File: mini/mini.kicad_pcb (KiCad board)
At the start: 2 copper layers, 1 part, among them U1 ESP32-WROOM-32E

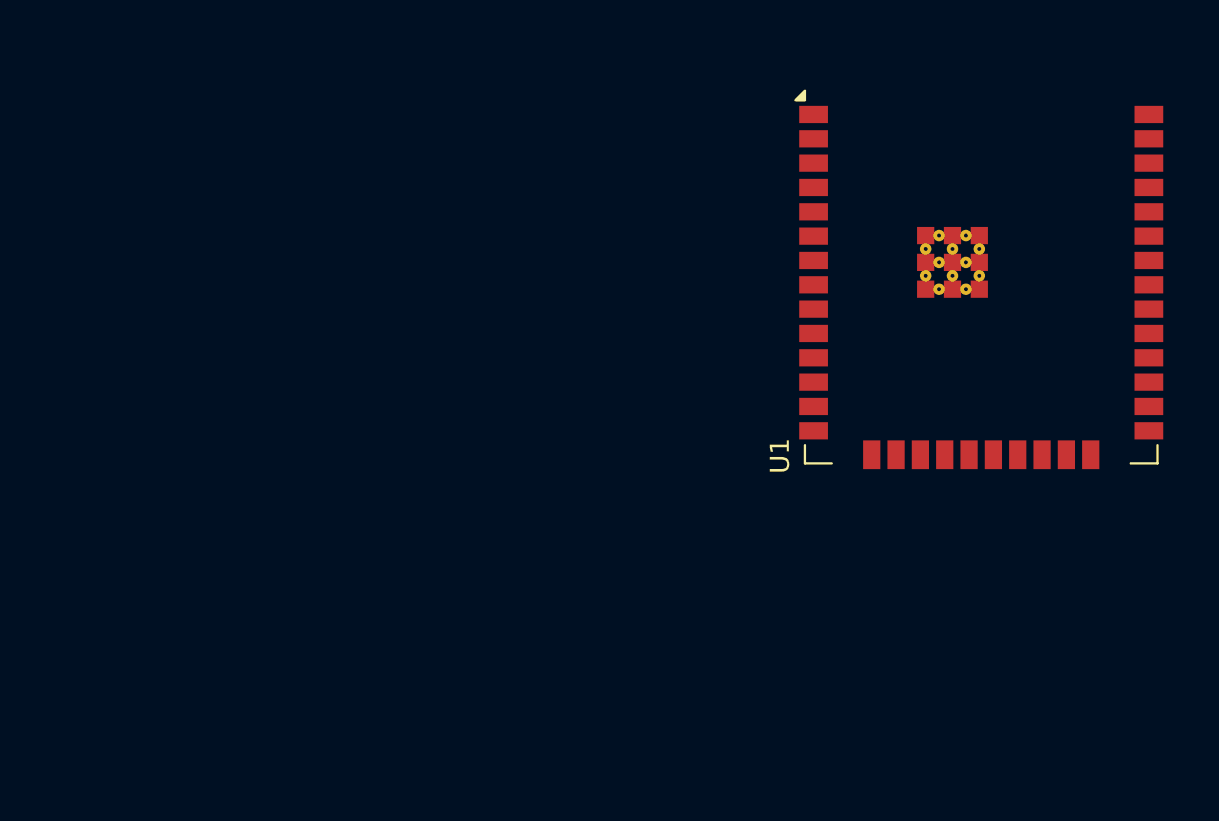
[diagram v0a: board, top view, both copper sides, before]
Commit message: Created power page schematic
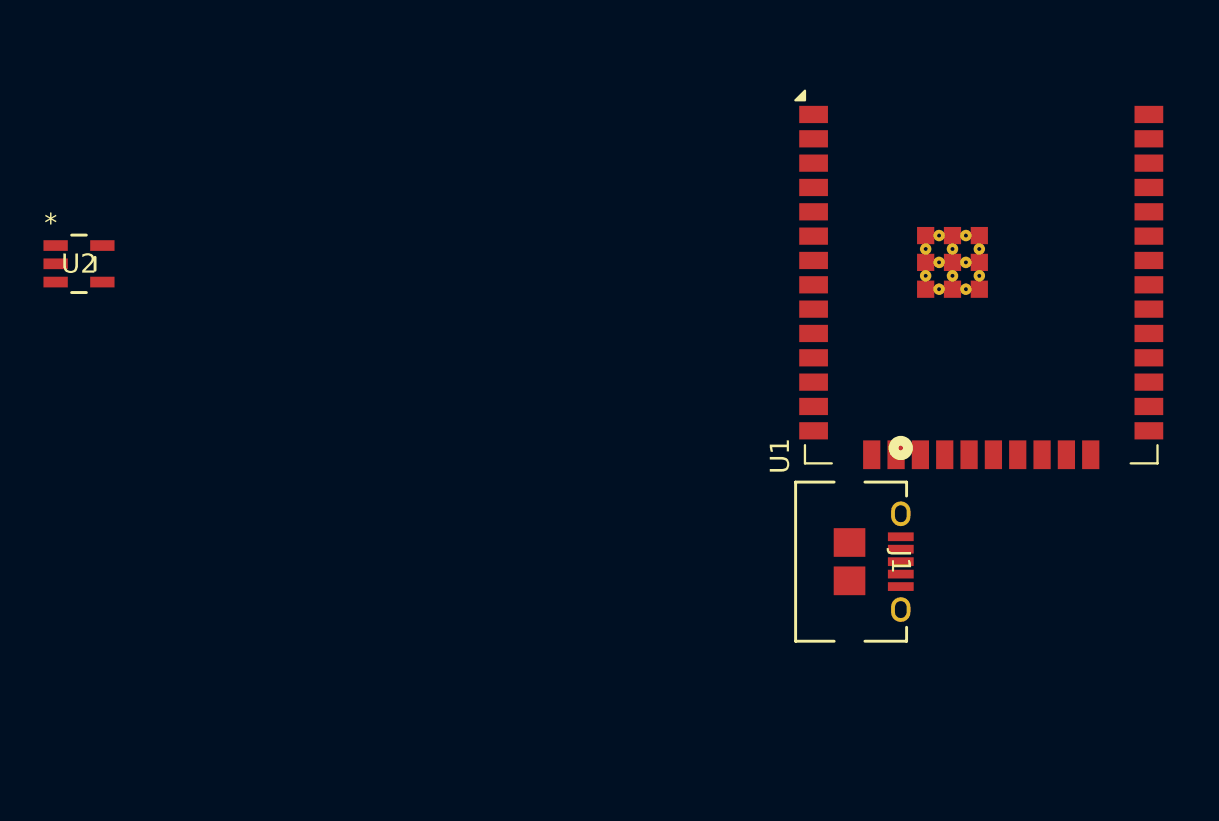
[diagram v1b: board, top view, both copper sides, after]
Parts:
- added J1: 10118194-0001LF, RVL:CONN_10118194-0001LF_AMP, F.Cu at (118.0, 124.1)
- added U2: LM3671MF-3.3/NOPB, RVL:MF05A, F.Cu at (77.7, 108.6)

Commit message: Added LED output
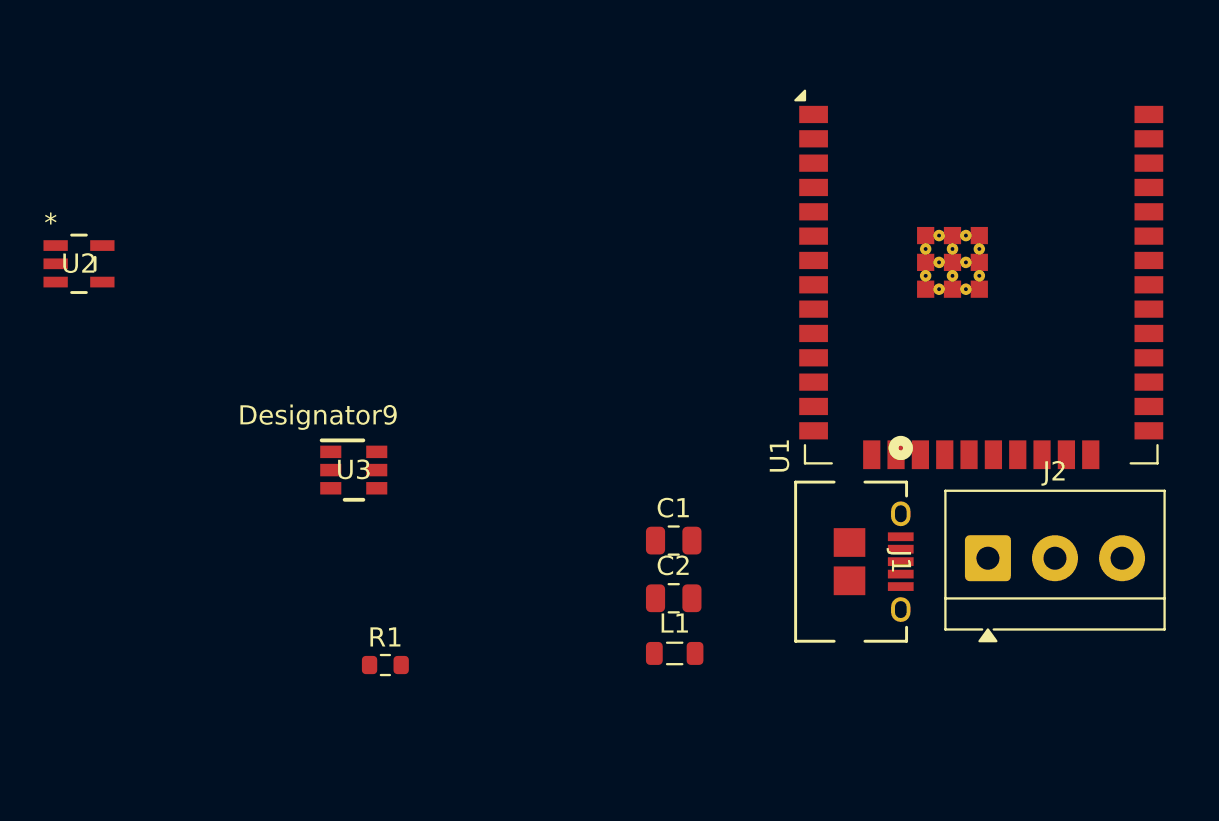
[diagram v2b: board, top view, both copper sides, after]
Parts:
- added C1: 4.7uF, Capacitor_SMD:C_0805_2012Metric, F.Cu at (108.7, 123.0)
- added C2: 10uF, Capacitor_SMD:C_0805_2012Metric, F.Cu at (108.7, 126.0)
- added J2: Screw_Terminal_01x03, TerminalBlock_4Ucon:TerminalBlock_4Ucon_1x03_P3.50mm_Horizontal, F.Cu at (125.1, 123.9)
- added L1: 2.2uH, Inductor_SMD:L_0805_2012Metric, F.Cu at (108.8, 128.9)
- added R1: 68, Resistor_SMD:R_0603_1608Metric, F.Cu at (93.7, 129.5)
- added U3: SN74LVC1T45DBVR, RVL:DBV0006A_N, F.Cu at (92.0, 119.3)
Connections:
- J1 pad 1: unconnected-(J1-Pad1) -> +5V
- J1 pad 2: unconnected-(J1-Pad2) -> USB_D-
- J1 pad 3: unconnected-(J1-Pad3) -> USB_D+
- J1 pad 5: unconnected-(J1-Pad5) -> GND
- U2 pad 1: unconnected-(U2-VIN-Pad1) -> +5V
- U2 pad 2: unconnected-(U2-GND-Pad2) -> GND
- U2 pad 3: unconnected-(U2-EN-Pad3) -> +5V
- U2 pad 4: unconnected-(U2-FB-Pad4) -> +3.3V
- U2 pad 5: unconnected-(U2-SW-Pad5) -> Net-(U2-SW)

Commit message: First draft of non-uart schematics
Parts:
- added C3: 1uf, Capacitor_SMD:C_0603_1608Metric, F.Cu at (91.5, 99.3)
- added D1: LED, LED_SMD:LED_0603_1608Metric, F.Cu at (101.0, 107.8)
- added R2: R, Resistor_SMD:R_0603_1608Metric, F.Cu at (102.7, 115.0)
- added R3: 12k, Resistor_SMD:R_0603_1608Metric, F.Cu at (95.2, 104.0)
- added R4: 5k, Resistor_SMD:R_0603_1608Metric, F.Cu at (91.7, 108.5)
- moved L1 6.11 mm to (108.9, 135.0)
- moved C2 2.98 mm to (108.7, 129.0)
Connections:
- U1 pad 1: unconnected-(U1-GND-Pad1) -> GND
- U1 pad 10: unconnected-(U1-IO25-Pad10) -> Net-(D1-A)
- U1 pad 15: unconnected-(U1-GND-Pad1) -> GND
- U1 pad 2: unconnected-(U1-VDD-Pad2) -> +3.3V
- U1 pad 25: unconnected-(U1-IO0-Pad25) -> IO0
- U1 pad 3: unconnected-(U1-EN-Pad3) -> EN
- U1 pad 34: unconnected-(U1-RXD0/IO3-Pad34) -> RXD
- U1 pad 35: unconnected-(U1-TXD0/IO1-Pad35) -> TXD
- U1 pad 38: unconnected-(U1-GND-Pad1) -> GND
- U1 pad 39: unconnected-(U1-GND-Pad1) -> GND
- U1 pad 9: unconnected-(U1-IO33-Pad9) -> LED_DATA

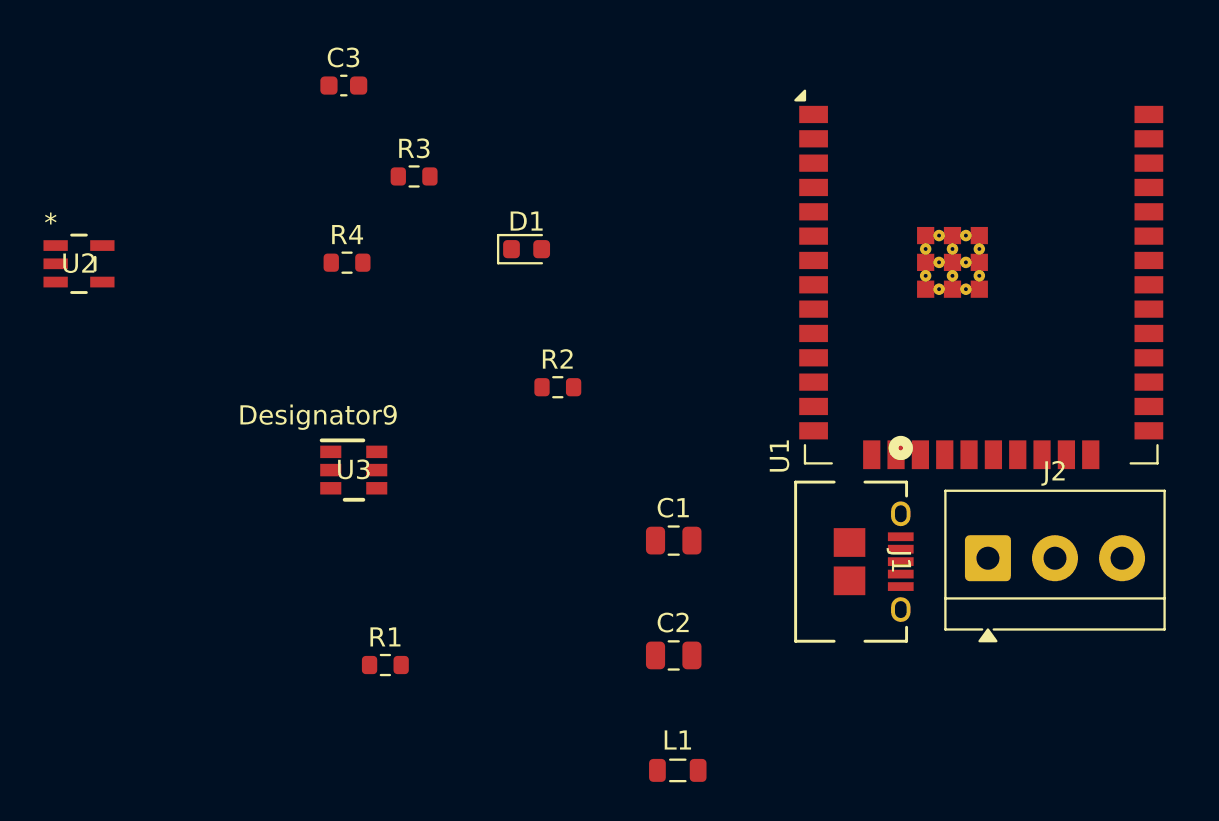
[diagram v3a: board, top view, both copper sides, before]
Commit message: First draft of mini board
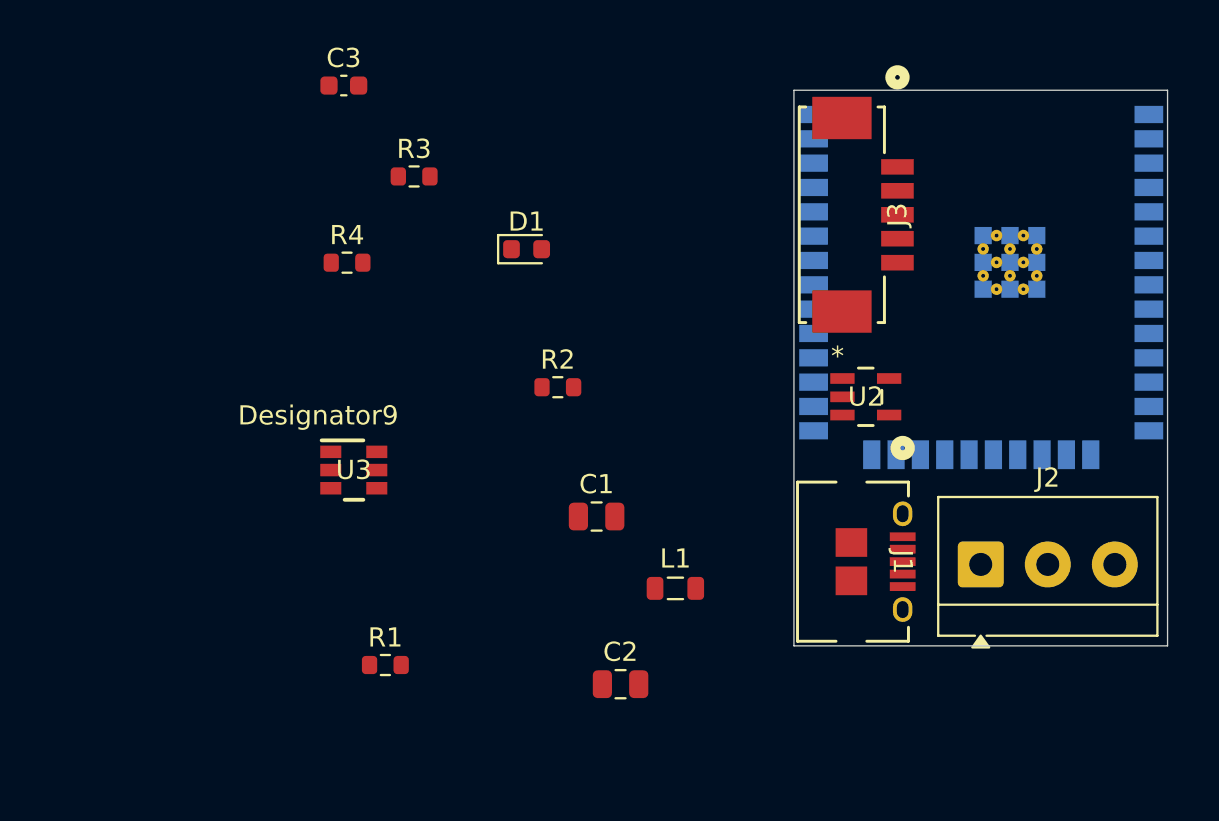
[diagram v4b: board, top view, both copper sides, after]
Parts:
- added J3: 532610571, RVL:CONN_532610001-SD_05_MOL, F.Cu at (117.5, 106.0)
- U1: moved to B.Cu
- moved U2 41.6 mm to (118.8, 115.5)
- moved L1 9.50 mm to (108.8, 125.5)
- moved C1 4.22 mm to (104.7, 121.8)
- moved C2 3.15 mm to (106.0, 130.5)
- moved J2 0.50 mm to (124.8, 124.2)
- moved J1 0.10 mm to (118.1, 124.1)
- turned U1 to 180 degrees
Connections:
- net EN renamed Net-(U1-EN)
- net IO0 renamed Net-(U1-IO0)
- J1 pad 2: USB_D- -> unconnected-(J1-Pad2)
- J1 pad 3: USB_D+ -> unconnected-(J1-Pad3)
- U1 pad 34: RXD -> Net-(U1-RXD0/IO3)
- U1 pad 35: TXD -> Net-(U1-TXD0/IO1)
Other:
- board outline added: 19.5 x 29 mm

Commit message: Finished regulator layout
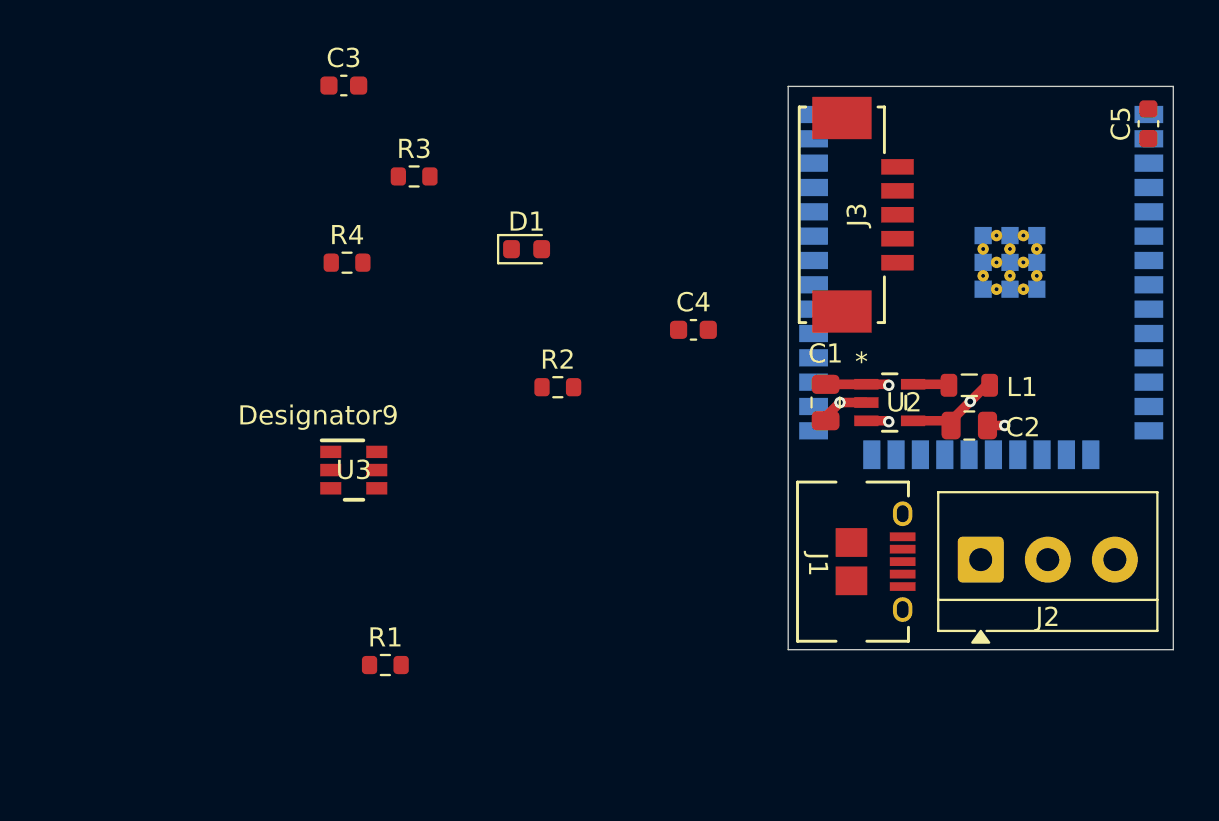
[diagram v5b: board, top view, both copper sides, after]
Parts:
- added C4: 0.1uF, Capacitor_SMD:C_0603_1608Metric, F.Cu at (109.8, 112.0)
- added C5: 0.1uF, Capacitor_SMD:C_0603_1608Metric, F.Cu at (133.5, 101.2)
- C3: value 1uf -> 1uF
- R2: value R -> 220
- R4: value 5k -> 10k
- moved C2 22.7 mm to (124.2, 117.0)
- moved L1 18.6 mm to (124.2, 114.9)
- moved C1 13.4 mm to (116.7, 115.8), turned to -90 degrees
- moved U2 1.29 mm to (120.0, 115.8)
- moved J2 0.25 mm to (124.8, 124.0)
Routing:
- net +3.3V: track 0.00 -> 5.12 mm, vias 0 -> 1
- net +5V: track 0.00 -> 4.51 mm, vias 0 -> 2
- net GND: track 0.00 -> 3.85 mm, vias 0 -> 2
- net Net-(U2-SW): track 0.00 -> 2.18 mm
- added copper zone on In2.Cu, net +3.3V
- added copper zone on In2.Cu, net +5V
- added copper zone on In1.Cu, net GND
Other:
- board size 19.5 x 29 mm -> 20.1 x 29.4 mm
- copper layers 2 -> 4

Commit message: Finished layout of the level translator
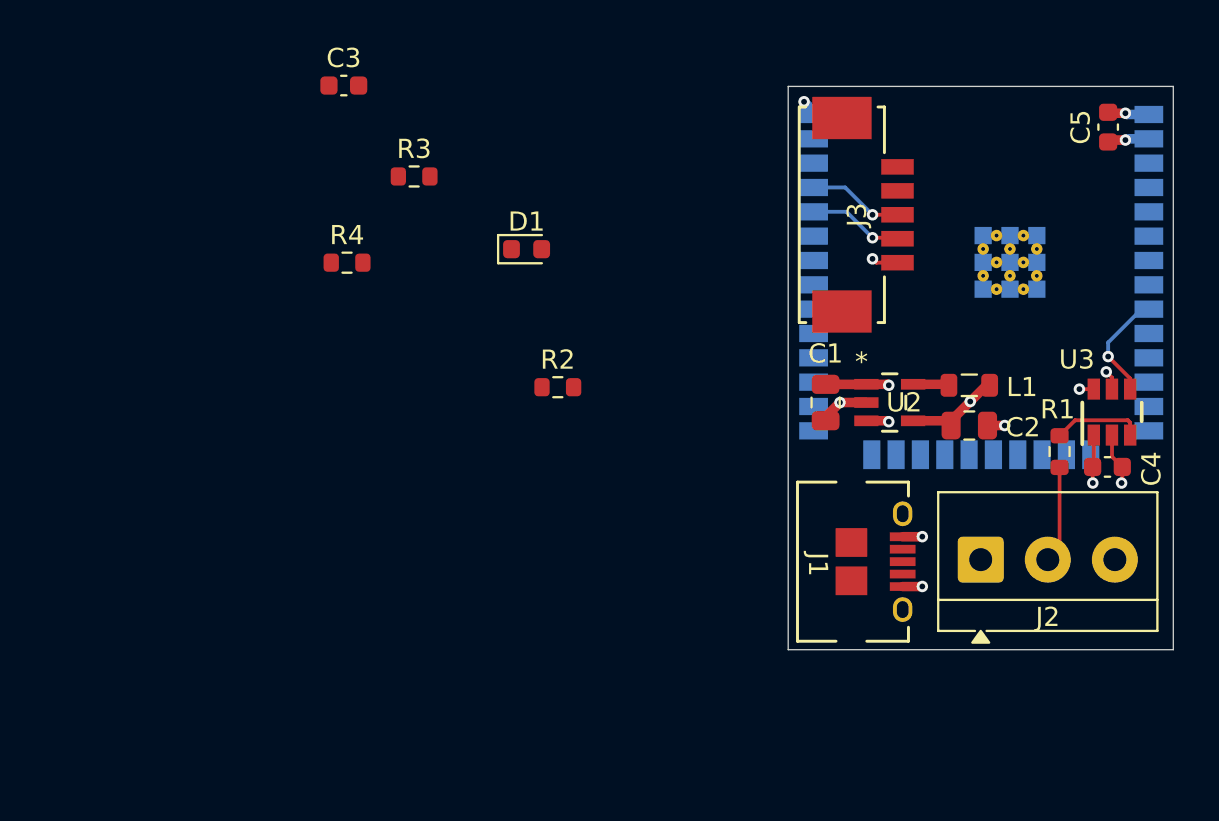
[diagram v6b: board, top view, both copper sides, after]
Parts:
- moved U3 39.7 mm to (131.6, 116.3), turned to 90 degrees
- moved R1 36.9 mm to (128.9, 118.4), turned to 90 degrees
- moved C4 22.8 mm to (131.4, 119.2)
- moved C5 2.11 mm to (131.4, 101.4)
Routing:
- net GND: track 3.85 -> 13.1 mm, vias 2 -> 8
- net LED_DATA: track 0.00 -> 5.76 mm, vias 0 -> 1
- net Net-(J2-Pin_2): track 0.00 -> 5.17 mm
- net Net-(U1-TXD0/IO1): track 0.00 -> 4.97 mm, vias 0 -> 1
- net Net-(U1-RXD0/IO3): track 0.00 -> 4.96 mm, vias 0 -> 1
- net Net-(U3-A): track 0.00 -> 4.73 mm
- net +5V: track 4.51 -> 8.07 mm, vias 2 -> 4
- net +3.3V: track 5.12 -> 8.06 mm, vias 1 -> 3

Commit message: First draft of finished mini board
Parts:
- removed R2: 220, Resistor_SMD:R_0603_1608Metric
- added R5: R, Resistor_SMD:R_0805_2012Metric, F.Cu at (123.4, 101.2)
- added R6: R, Resistor_SMD:R_0805_2012Metric, F.Cu at (127.0, 101.2)
- added R7: R, Resistor_SMD:R_0805_2012Metric, F.Cu at (123.1, 108.5)
- C3, C4, C5: footprint Capacitor_SMD:C_0603_1608Metric -> Capacitor_SMD:C_0805_2012Metric
- D1: value LED -> LED_RGB; footprint LED_SMD:LED_0603_1608Metric -> RVL:LED_RGB_PLCC-6
- R1, R3, R4: footprint Resistor_SMD:R_0603_1608Metric -> Resistor_SMD:R_0805_2012Metric
- moved C3 40.3 mm to (131.4, 105.1), turned to -90 degrees
- moved R3 34.0 mm to (129.2, 105.1), turned to 90 degrees
- moved R4 27.9 mm to (117.6, 118.7), turned to 180 degrees
- moved D1 24.5 mm to (125.3, 104.5)
- moved U3 0.50 mm to (131.6, 115.8)
- moved C4 0.37 mm to (131.7, 119.0)
- moved C5 0.30 mm to (131.1, 101.4)
- moved R1 0.26 mm to (128.6, 118.4)
- moved J2 0.17 mm to (124.8, 124.2)
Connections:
- D1 pad 1: Net-(D1-K) -> Net-(D1-RA)
- D1 pad 2: Net-(D1-A) -> Net-(D1-RK)
- U1 pad 10: Net-(D1-A) -> unconnected-(U1-IO25-Pad10)
- U1 pad 33: unconnected-(U1-IO21-Pad33) -> Net-(D1-BA)
- U1 pad 36: unconnected-(U1-IO22-Pad36) -> Net-(D1-GA)
- U1 pad 37: unconnected-(U1-IO23-Pad37) -> Net-(D1-RA)
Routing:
- net Net-(U1-EN): track 0.00 -> 20.9 mm, vias 0 -> 1
- net Net-(U1-IO0): track 0.00 -> 19.5 mm, vias 0 -> 2
- net Net-(D1-BA): track 0.00 -> 11.8 mm, vias 0 -> 1
- net Net-(D1-RA): track 0.00 -> 8.29 mm, vias 0 -> 1
- net Net-(D1-GA): track 0.00 -> 8.22 mm, vias 0 -> 1
- net GND: track 13.1 -> 19.9 mm, vias 8 -> 13
- net +3.3V: track 8.06 -> 13.0 mm, vias 3 -> 4
- net Net-(D1-BK): track 0.00 -> 4.57 mm
- net Net-(D1-GK): track 0.00 -> 4.52 mm
- net Net-(D1-RK): track 0.00 -> 3.45 mm
- net LED_DATA: track 5.76 -> 4.73 mm
- net +5V: track 8.07 -> 8.79 mm
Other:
- board text added: "RVL Mini v1.0 © Bryan Hughes"
